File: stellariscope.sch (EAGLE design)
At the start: 29 parts, among them U1 74238, U2 74238, U3 TLC5947PWP, U4 TLC59213, U5 741G79DCT, U6 74AHC1G126DBV, U7 74AHC1G126DBV, U8 74AHC1G32DBV, U9 74AHC1G32DBV

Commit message: This update fixes the issues with the board counting logic in the first edition. It also adds a driver to the XLAT line in order to prevent fanout problems in large array. This version has not been built and is unlikely to be built.
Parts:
- added C8: 100n, resistor:C-USC0603
- added U10: 74AHC1G126DBV, 74xx-little-us:74AHC1G126DBV
- C1, C2, C3, C4, C5, C7: value (none) -> 100n; PARTNO (none) -> CC0603KRX7R9BB104
- C6: value (none) -> 1u; PARTNO (none) -> C1608X5R1E105M
- D1: BOM (none) -> EXCLUDE; PARTNO (none) -> *
- HIN: PARTNO (none) -> 87760-121
- HOUT: PARTNO (none) -> 87264-125
- J1: PARTNO (none) -> S2B-PH-SM4-TB(LF)(SN)
- LAUNCHPAD: BOM (none) -> EXCLUDE
- R1: value (none) -> 2K7; PARTNO (none) -> RMCF0603FT2K70
- R2, R3, R4: value (none) -> 10K; PARTNO (none) -> RMCF0603FT10K0
- U1, U2: PARTNO (none) -> SN74AHC138PWR
- U3: PARTNO (none) -> TLC5947DAP
- U4: PARTNO (none) -> TLC59213IPWR
- U5: PARTNO (none) -> SN74LVC2G79DCTR
- U6, U7: PARTNO (none) -> SN74LVC1G126DBVR
- U8, U9: PARTNO (none) -> SN74LVC1G32QDBVRQ1
- VIN1, VIN2: PARTNO (none) -> 87760-081
- VOUT1, VOUT2: PARTNO (none) -> 87264-085
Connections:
- net +3V3: now also C8.1, U10A.OE, U10P.VCC
- net GND: now also C8.2, U10P.GND
- net HCNT_OUT: no longer HIN-11.S
- net N$28: now also HOUT-3.S, U10A.O, VOUT1-7.S; no longer LAUNCHPAD.P2.7, U5A.CLK, U5B.CLK
- net N$37: now also HIN-11.S
- net N$38: now also VIN2-6.S
- net VCNT_OUT: no longer VIN2-6.S
- net XLAT: now also U10A.I, U5A.CLK, U5B.CLK; no longer HOUT-3.S, VOUT1-7.S
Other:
- moved on the sheet: C1, C2, C3, C4, C5, C6, C7, D1ANODE, D1BLUE, D1GREEN, D1RED, HIN-1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

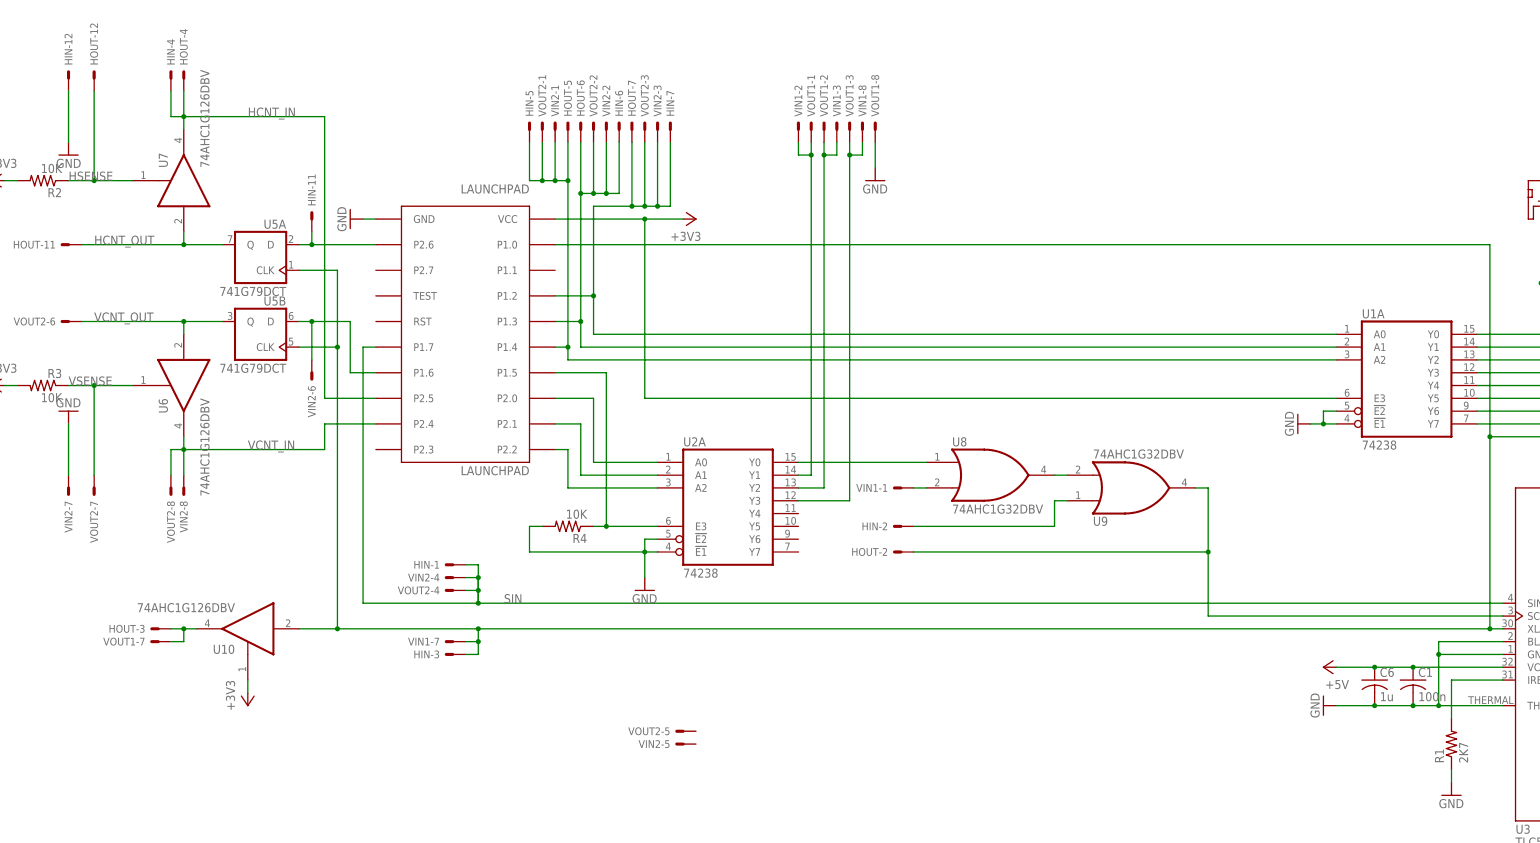
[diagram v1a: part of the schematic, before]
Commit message: -- Rotated Launchpad footprint to align with LED array -- Swapped vertical connectors to improve routing post-rotation -- Switched power on TLC5947 to 3V3, in order to accomodate logic levels -- Relocated power and horizontal connectors to midline (more or less) -- Added mounting holes
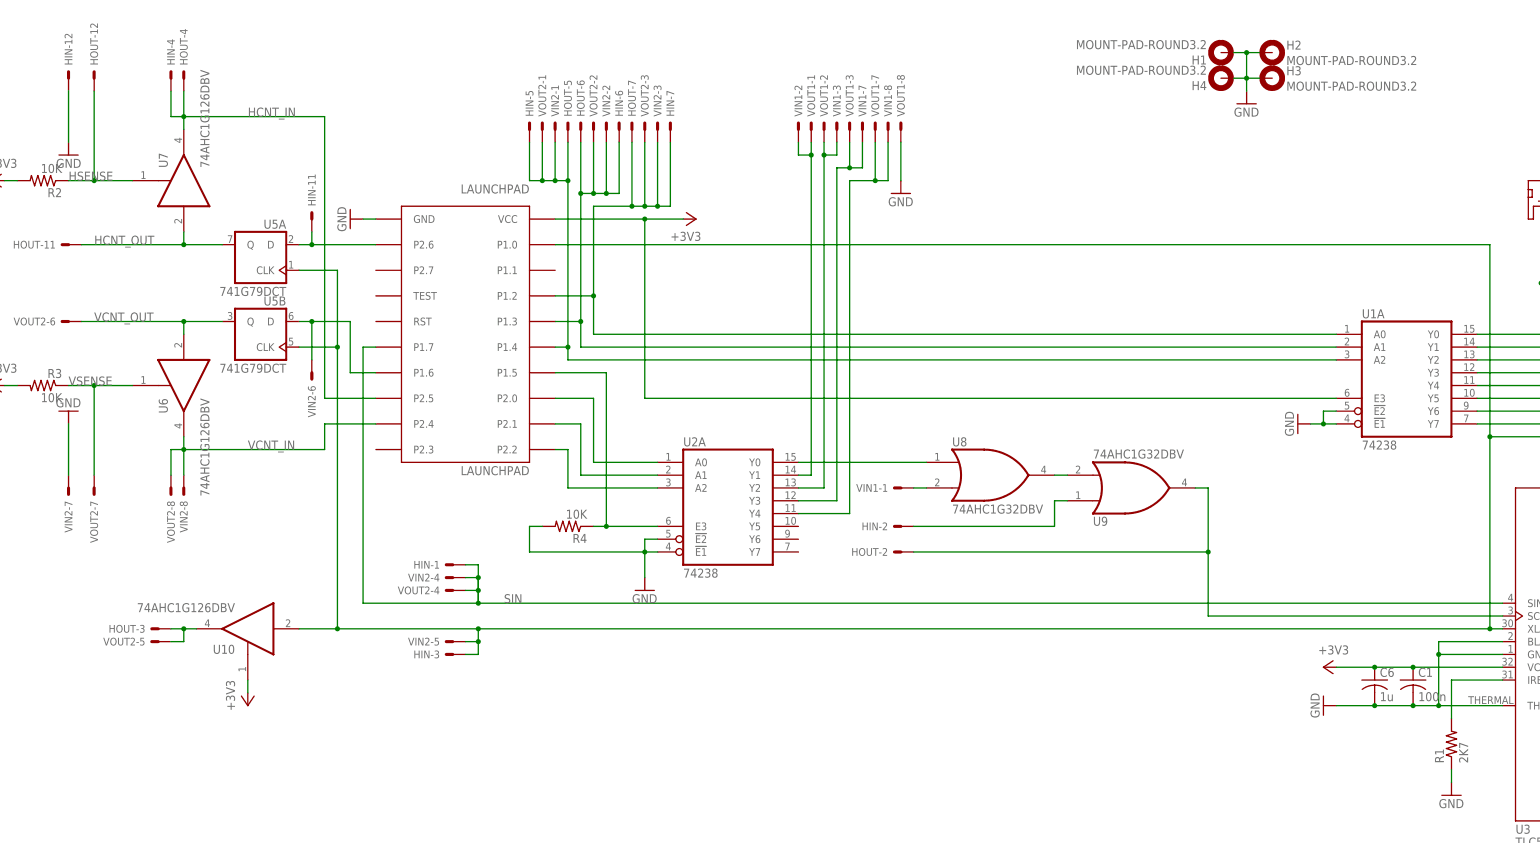
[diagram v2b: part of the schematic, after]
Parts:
- added H1, H2, H3, H4: MOUNT-PAD-ROUND3.2, holes:MOUNT-PAD-ROUND3.2
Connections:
- removed net N$28: HOUT-3.S, U10A.O, VOUT1-7.S
- new net N$41: U2A.Y4, VIN1-8.S, VOUT1-7.S
- new net XLAT_OUT: HOUT-3.S, U10A.O, VOUT2-5.S
- net +3V3: now also C1.1, C6.1, U3.VCC
- net +5V: no longer C1.1, C6.1, U3.VCC
- net GND: now also H1.MOUNT, H2.MOUNT, H3.MOUNT, H4.MOUNT
- net N$27: now also VIN1-7.S; no longer VIN1-8.S
- net XLAT: now also VIN2-5.S; no longer VIN1-7.S
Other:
- moved on the sheet: VIN1-7, VIN1-8, VIN2-5, VOUT1-7, VOUT1-8, VOUT2-5
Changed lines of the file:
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@@
 <part name="+3V4" library="supply1" deviceset="+3V3" device=""/>
 <part name="P+1" library="supply1" deviceset="+5V" device=""/>
-<part name="P+2" library="supply1" deviceset="+5V" device=""/>
 <part name="GND1" library="supply1" deviceset="GND" device=""/>
 <part name="GND2" library="supply1" deviceset="GND" device=""/>
@@
 <attribute name="PARTNO" value="CC0603KRX7R9BB104"/>
 </part>
+<part name="H1" library="holes" deviceset="MOUNT-PAD-ROUND" device="3.2"/>
+<part name="H2" library="holes" deviceset="MOUNT-PAD-ROUND" device="3.2"/>
+<part name="H3" library="holes" deviceset="MOUNT-PAD-ROUND" device="3.2"/>
+<part name="H4" library="holes" deviceset="MOUNT-PAD-ROUND" device="3.2"/>
+<part name="GND18" library="supply1" deviceset="GND" device=""/>
+<part name="+3V12" library="supply1" deviceset="+3V3" device=""/>
 </parts>
 <sheets>
@@
 <instance part="+3V4" gate="G$1" x="134.62" y="68.58"/>
 <instance part="P+1" gate="1" x="347.98" y="193.04"/>
-<instance part="P+2" gate="1" x="279.4" y="109.22" rot="R90"/>
 <instance part="GND1" gate="1" x="347.98" y="154.94" rot="R90"/>
 <instance part="GND2" gate="1" x="279.4" y="101.6" rot="R270"/>
@@
 <attribute name="NAME" x="215.9" y="64.262" size="1.524" layer="95" rot="MR180"/>
 </instance>
-<instance part="VIN1" gate="-7" x="106.68" y="114.3" smashed="yes" rot="R180">
-<attribute name="NAME" x="104.14" y="115.062" size="1.524" layer="95" rot="R180"/>
-</instance>
-<instance part="VIN1" gate="-8" x="187.96" y="215.9" smashed="yes" rot="R90">
+<instance part="VIN1" gate="-7" x="187.96" y="215.9" smashed="yes" rot="R90">
 <attribute name="NAME" x="188.722" y="218.44" size="1.524" layer="95" rot="R90"/>
+</instance>
+<instance part="VIN1" gate="-8" x="193.04" y="215.9" smashed="yes" rot="R90">
+<attribute name="NAME" x="193.802" y="218.44" size="1.524" layer="95" rot="R90"/>
 </instance>
 <instance part="VIN2" gate="-1" x="127" y="215.9" smashed="yes" rot="R90">
@@
 <attribute name="NAME" x="104.14" y="127.762" size="1.524" layer="95" rot="R180"/>
 </instance>
-<instance part="VIN2" gate="-5" x="152.4" y="93.98" smashed="yes" rot="R180">
-<attribute name="NAME" x="149.86" y="94.742" size="1.524" layer="95" rot="R180"/>
+<instance part="VIN2" gate="-5" x="106.68" y="114.3" smashed="yes" rot="R180">
+<attribute name="NAME" x="104.14" y="115.062" size="1.524" layer="95" rot="R180"/>
 </instance>
 <instance part="VIN2" gate="-6" x="78.74" y="167.64" smashed="yes" rot="R270">
@@
 <attribute name="NAME" x="205.74" y="64.262" size="1.524" layer="95" rot="R180"/>
 </instance>
-<instance part="VOUT1" gate="-7" x="48.26" y="114.3" smashed="yes" rot="R180">
-<attribute name="NAME" x="45.72" y="115.062" size="1.524" layer="95" rot="R180"/>
-</instance>
-<instance part="VOUT1" gate="-8" x="190.5" y="215.9" smashed="yes" rot="R90">
+<instance part="VOUT1" gate="-7" x="190.5" y="215.9" smashed="yes" rot="R90">
 <attribute name="NAME" x="191.262" y="218.44" size="1.524" layer="95" rot="R90"/>
+</instance>
+<instance part="VOUT1" gate="-8" x="195.58" y="215.9" smashed="yes" rot="R90">
+<attribute name="NAME" x="196.342" y="218.44" size="1.524" layer="95" rot="R90"/>
 </instance>
 <instance part="VOUT2" gate="-1" x="124.46" y="215.9" smashed="yes" rot="MR90">
@@
 <attribute name="NAME" x="104.14" y="125.222" size="1.524" layer="95" rot="R180"/>
 </instance>
-<instance part="VOUT2" gate="-5" x="152.4" y="96.52" smashed="yes" rot="R180">
-<attribute name="NAME" x="149.86" y="97.282" size="1.524" layer="95" rot="R180"/>
+<instance part="VOUT2" gate="-5" x="48.26" y="114.3" smashed="yes" rot="R180">
+<attribute name="NAME" x="45.72" y="115.062" size="1.524" layer="95" rot="R180"/>
 </instance>
 <instance part="VOUT2" gate="-6" x="30.48" y="177.8" smashed="yes" rot="R180">
@@
 <attribute name="NAME" x="50.038" y="142.24" size="1.524" layer="95" rot="R270"/>
 </instance>
-<instance part="GND11" gate="1" x="190.5" y="205.74"/>
+<instance part="GND11" gate="1" x="195.58" y="203.2"/>
 <instance part="U9" gate="A" x="241.3" y="144.78" rot="MR180">
 <attribute name="PARTNO" x="241.3" y="144.78" size="1.778" layer="96" display="off"/>
@@
 <attribute name="PARTNO" x="58.42" y="50.8" size="1.778" layer="96" display="off"/>
 </instance>
+<instance part="H1" gate="G$1" x="259.08" y="231.14" rot="R180"/>
+<instance part="H2" gate="G$1" x="269.24" y="231.14"/>
+<instance part="H3" gate="G$1" x="269.24" y="226.06"/>
+<instance part="H4" gate="G$1" x="259.08" y="226.06" rot="R180"/>
+<instance part="GND18" gate="1" x="264.16" y="220.98"/>
+<instance part="+3V12" gate="G$1" x="279.4" y="109.22" rot="MR270"/>
 </instances>
 <busses>
@@
 <junction x="66.04" y="63.5"/>
 </segment>
-</net>
-<net name="+5V" class="0">
 <segment>
 <pinref part="U3" gate="G$1" pin="VCC"/>
-<pinref part="P+2" gate="1" pin="+5V"/>
 <wire x1="281.94" y1="109.22" x2="289.56" y2="109.22" width="0.1524" layer="91"/>
 <pinref part="C1" gate="G$1" pin="1"/>
@@
 <pinref part="C6" gate="G$1" pin="1"/>
 <junction x="289.56" y="109.22"/>
-</segment>
+<pinref part="+3V12" gate="G$1" pin="+3V3"/>
+</segment>
+</net>
+<net name="+5V" class="0">
 <segment>
 <pinref part="U4" gate="A" pin="!CLR!"/>
@@
 </segment>
 <segment>
-<pinref part="VOUT1" gate="-8" pin="S"/>
-<pinref part="GND11" gate="1" pin="GND"/>
-<wire x1="190.5" y1="208.28" x2="190.5" y2="213.36" width="0.1524" layer="91"/>
-</segment>
-<segment>
 <pinref part="HIN" gate="-12" pin="S"/>
 <pinref part="GND15" gate="1" pin="GND"/>
@@
 <wire x1="58.42" y1="38.1" x2="58.42" y2="45.72" width="0.1524" layer="91"/>
 <junction x="66.04" y="38.1"/>
+</segment>
+<segment>
+<pinref part="VOUT1" gate="-8" pin="S"/>
+<pinref part="GND11" gate="1" pin="GND"/>
+<wire x1="195.58" y1="205.74" x2="195.58" y2="213.36" width="0.1524" layer="91"/>
+</segment>
+<segment>
+<pinref part="H2" gate="G$1" pin="MOUNT"/>
+<pinref part="H1" gate="G$1" pin="MOUNT"/>
+<wire x1="261.62" y1="231.14" x2="264.16" y2="231.14" width="0.1524" layer="91"/>
+<pinref part="H3" gate="G$1" pin="MOUNT"/>
+<pinref part="H4" gate="G$1" pin="MOUNT"/>
+<wire x1="264.16" y1="231.14" x2="266.7" y2="231.14" width="0.1524" layer="91"/>
+<wire x1="261.62" y1="226.06" x2="264.16" y2="226.06" width="0.1524" layer="91"/>
+<wire x1="264.16" y1="226.06" x2="266.7" y2="226.06" width="0.1524" layer="91"/>
+<wire x1="264.16" y1="231.14" x2="264.16" y2="226.06" width="0.1524" layer="91"/>
+<wire x1="264.16" y1="226.06" x2="264.16" y2="223.52" width="0.1524" layer="91"/>
+<pinref part="GND18" gate="1" pin="GND"/>
+<junction x="264.16" y="226.06"/>
+<junction x="264.16" y="231.14"/>
 </segment>
 </net>
@@
 <pinref part="HIN" gate="-3" pin="S"/>
 <wire x1="109.22" y1="111.76" x2="111.76" y2="111.76" width="0.1524" layer="91"/>
-<pinref part="VIN1" gate="-7" pin="S"/>
 <wire x1="111.76" y1="111.76" x2="111.76" y2="114.3" width="0.1524" layer="91"/>
 <wire x1="111.76" y1="114.3" x2="111.76" y2="116.84" width="0.1524" layer="91"/>
@@
 <wire x1="83.82" y1="116.84" x2="76.2" y2="116.84" width="0.1524" layer="91"/>
 <junction x="83.82" y="116.84"/>
+<pinref part="VIN2" gate="-5" pin="S"/>
 </segment>
 </net>
@@
 <net name="N$27" class="0">
 <segment>
-<pinref part="VIN1" gate="-8" pin="S"/>
-<wire x1="187.96" y1="213.36" x2="187.96" y2="210.82" width="0.1524" layer="91"/>
 <pinref part="VOUT1" gate="-3" pin="S"/>
-<wire x1="187.96" y1="210.82" x2="185.42" y2="210.82" width="0.1524" layer="91"/>
-<wire x1="185.42" y1="210.82" x2="185.42" y2="213.36" width="0.1524" layer="91"/>
+<wire x1="187.96" y1="208.28" x2="185.42" y2="208.28" width="0.1524" layer="91"/>
+<wire x1="185.42" y1="208.28" x2="185.42" y2="213.36" width="0.1524" layer="91"/>
 <pinref part="U2" gate="A" pin="Y3"/>
-<wire x1="175.26" y1="142.24" x2="185.42" y2="142.24" width="0.1524" layer="91"/>
-<wire x1="185.42" y1="142.24" x2="185.42" y2="210.82" width="0.1524" layer="91"/>
-<junction x="185.42" y="210.82"/>
-</segment>
-</net>
-<net name="N$28" class="0">
+<wire x1="175.26" y1="142.24" x2="182.88" y2="142.24" width="0.1524" layer="91"/>
+<wire x1="182.88" y1="142.24" x2="182.88" y2="208.28" width="0.1524" layer="91"/>
+<wire x1="182.88" y1="208.28" x2="185.42" y2="208.28" width="0.1524" layer="91"/>
+<junction x="185.42" y="208.28"/>
+<wire x1="187.96" y1="208.28" x2="187.96" y2="213.36" width="0.1524" layer="91"/>
+<pinref part="VIN1" gate="-7" pin="S"/>
+</segment>
+</net>
+<net name="XLAT_OUT" class="0">
 <segment>
 <pinref part="U10" gate="A" pin="O"/>
 <pinref part="HOUT" gate="-3" pin="S"/>
 <wire x1="55.88" y1="116.84" x2="53.34" y2="116.84" width="0.1524" layer="91"/>
-<pinref part="VOUT1" gate="-7" pin="S"/>
 <wire x1="53.34" y1="116.84" x2="50.8" y2="116.84" width="0.1524" layer="91"/>
 <wire x1="50.8" y1="114.3" x2="53.34" y2="114.3" width="0.1524" layer="91"/>
 <wire x1="53.34" y1="114.3" x2="53.34" y2="116.84" width="0.1524" layer="91"/>
 <junction x="53.34" y="116.84"/>
-</segment>
-</net>
+<pinref part="VOUT2" gate="-5" pin="S"/>
+</segment>
+</net>
+<net name="N$41" class="0">
+<segment>
+<pinref part="VIN1" gate="-8" pin="S"/>
+<wire x1="193.04" y1="213.36" x2="193.04" y2="205.74" width="0.1524" layer="91"/>
+<wire x1="193.04" y1="205.74" x2="190.5" y2="205.74" width="0.1524" layer="91"/>
+<wire x1="190.5" y1="205.74" x2="185.42" y2="205.74" width="0.1524" layer="91"/>
+<wire x1="185.42" y1="205.74" x2="185.42" y2="139.7" width="0.1524" layer="91"/>
+<pinref part="U2" gate="A" pin="Y4"/>
+<wire x1="185.42" y1="139.7" x2="175.26" y2="139.7" width="0.1524" layer="91"/>
+<wire x1="190.5" y1="205.74" x2="190.5" y2="213.36" width="0.1524" layer="91"/>
+<junction x="190.5" y="205.74"/>
+<pinref part="VOUT1" gate="-7" pin="S"/>
+</segment>
+</net>

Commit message: -- Moved the old demo code to led test -- First commit of new demo code -- Updated hardware design 	-- Add 10 uF decoupling caps for board & anode drive 	-- tied latch and blank lines together
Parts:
- removed H4: MOUNT-PAD-ROUND3.2, holes:MOUNT-PAD-ROUND3.2
- removed J1: (no value), SparkFun-Connectors:JST_2MM_MALE
- added JP1: (no value), pinhead:PINHD-1X3
- added JP2: (no value), pinhead-1:PINHD-1X2_2.54-90°
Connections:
- net +5V: now also JP1.3, JP2.1; no longer J1.+
- net GND: now also JP1.1, JP1.2, JP2.2; no longer H4.MOUNT, J1.-, U3.BLANK
- net XLAT: now also U3.BLANK
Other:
- moved on the sheet: D1ANODE, D1BLUE, D1GREEN, D1RED, HOUT-1, U4

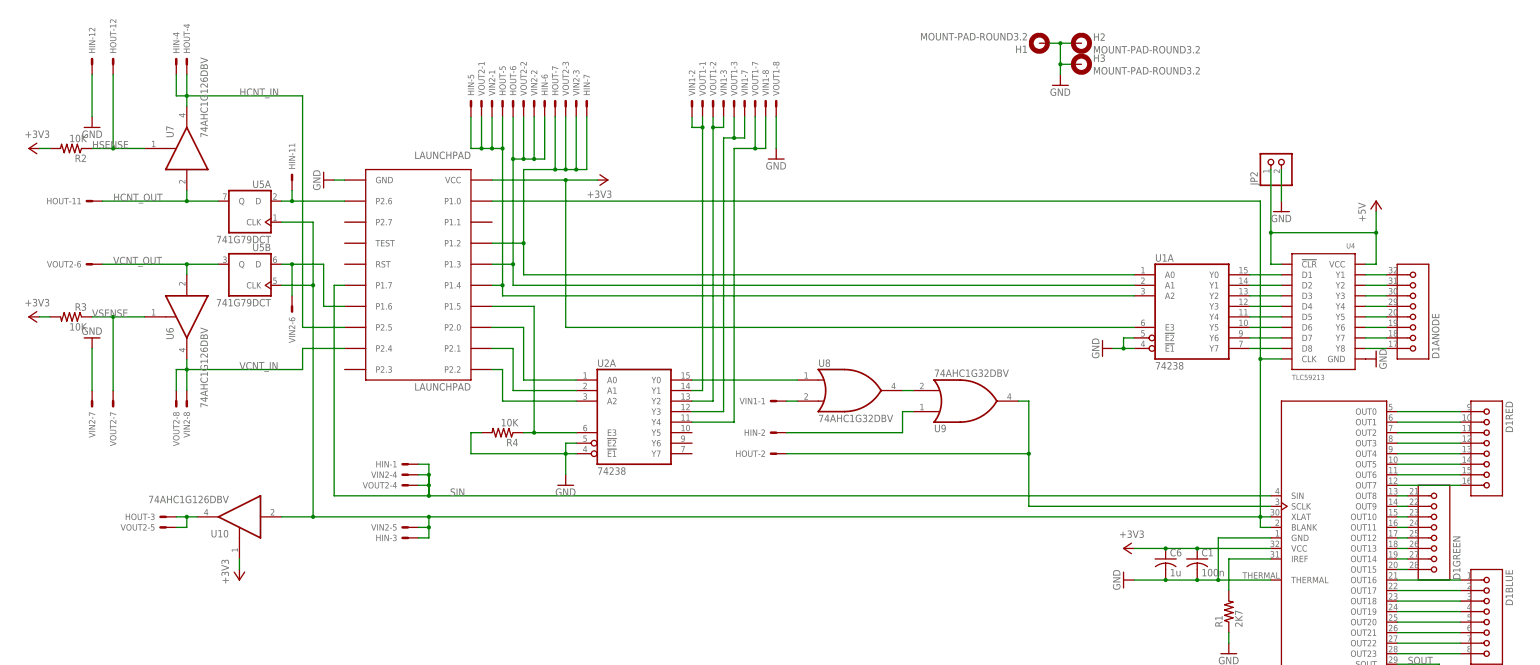
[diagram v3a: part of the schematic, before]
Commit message: -- Modified pinout to allow UART to function correctly
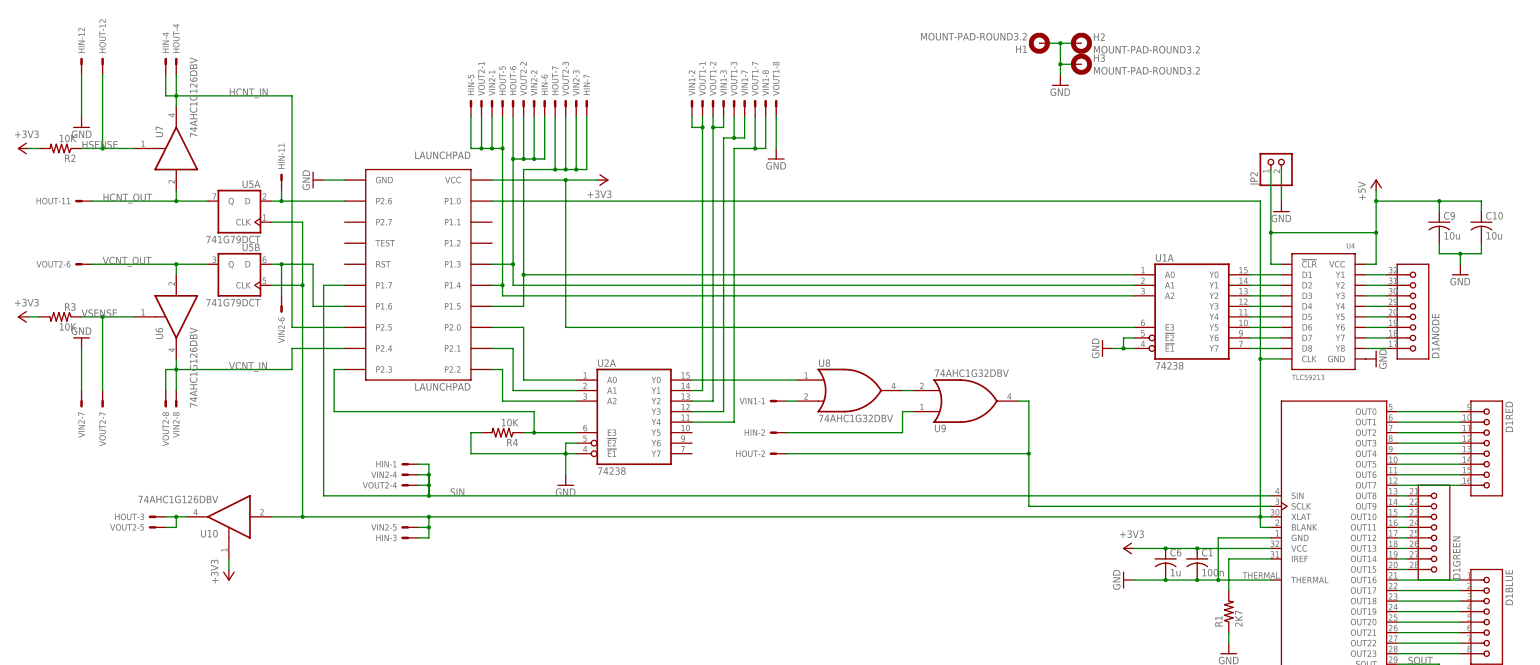
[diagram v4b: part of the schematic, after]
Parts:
- added C10, C9: 10u, resistor:C-USC1210
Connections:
- net +5V: now also C10.1, C9.1
- net GND: now also C10.2, C9.2
- net N$29: now also LAUNCHPAD.P2.3; no longer LAUNCHPAD.P1.5
- net N$36: now also LAUNCHPAD.P1.5; no longer LAUNCHPAD.P1.2
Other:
- moved on the sheet: HIN-11, HIN-12, HIN-4, HOUT-11, HOUT-12, HOUT-3, HOUT-4, R2, R3, U10, U5A, U5B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
